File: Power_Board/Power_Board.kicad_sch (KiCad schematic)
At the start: 21 parts, among them J1 Conn_01x10_Female, J2 Conn_01x10_Female, J3 Conn_01x06_Male, J4 Screw_Terminal_01x02, J5 Screw_Terminal_01x02, J6 Conn_01x02_Male

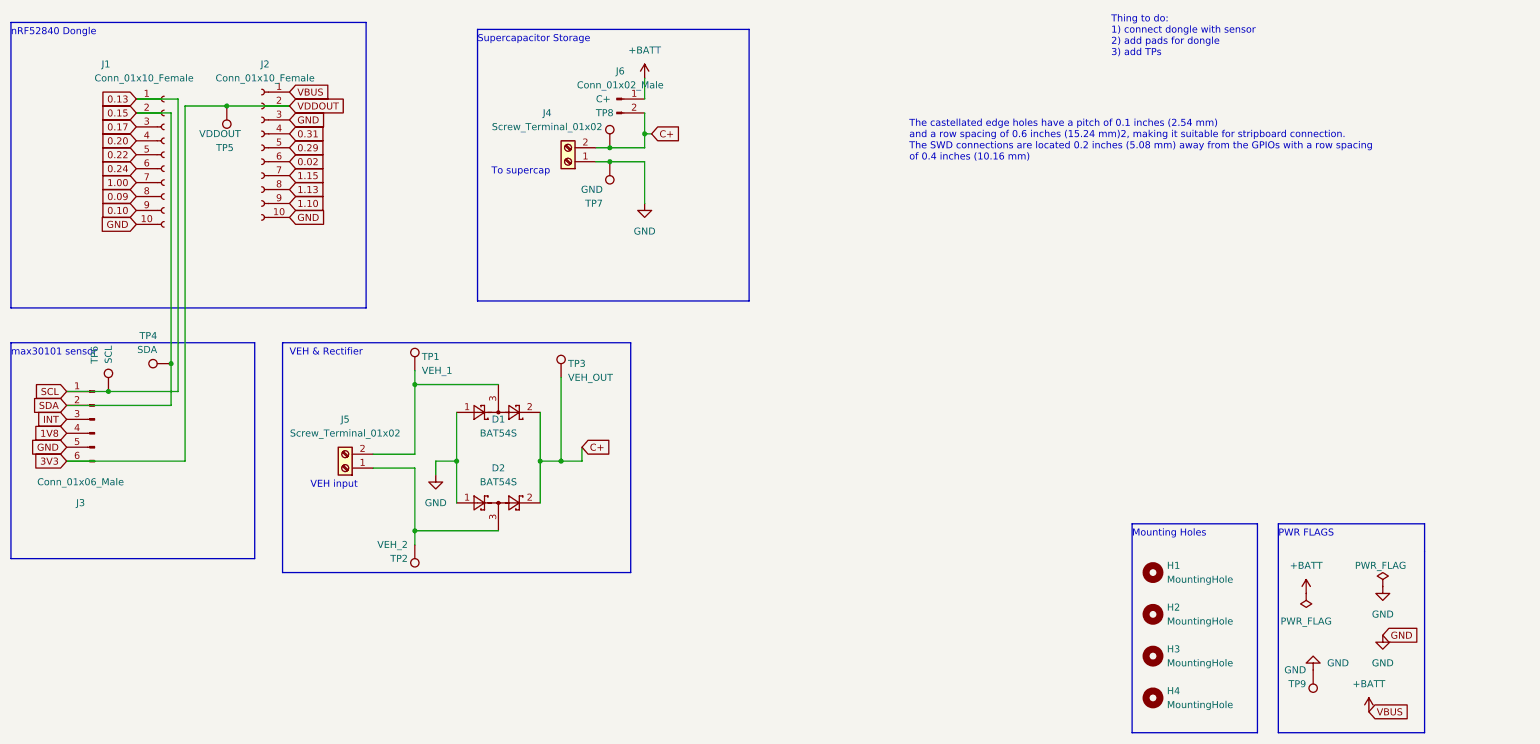
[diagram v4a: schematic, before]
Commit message: silkscreen added
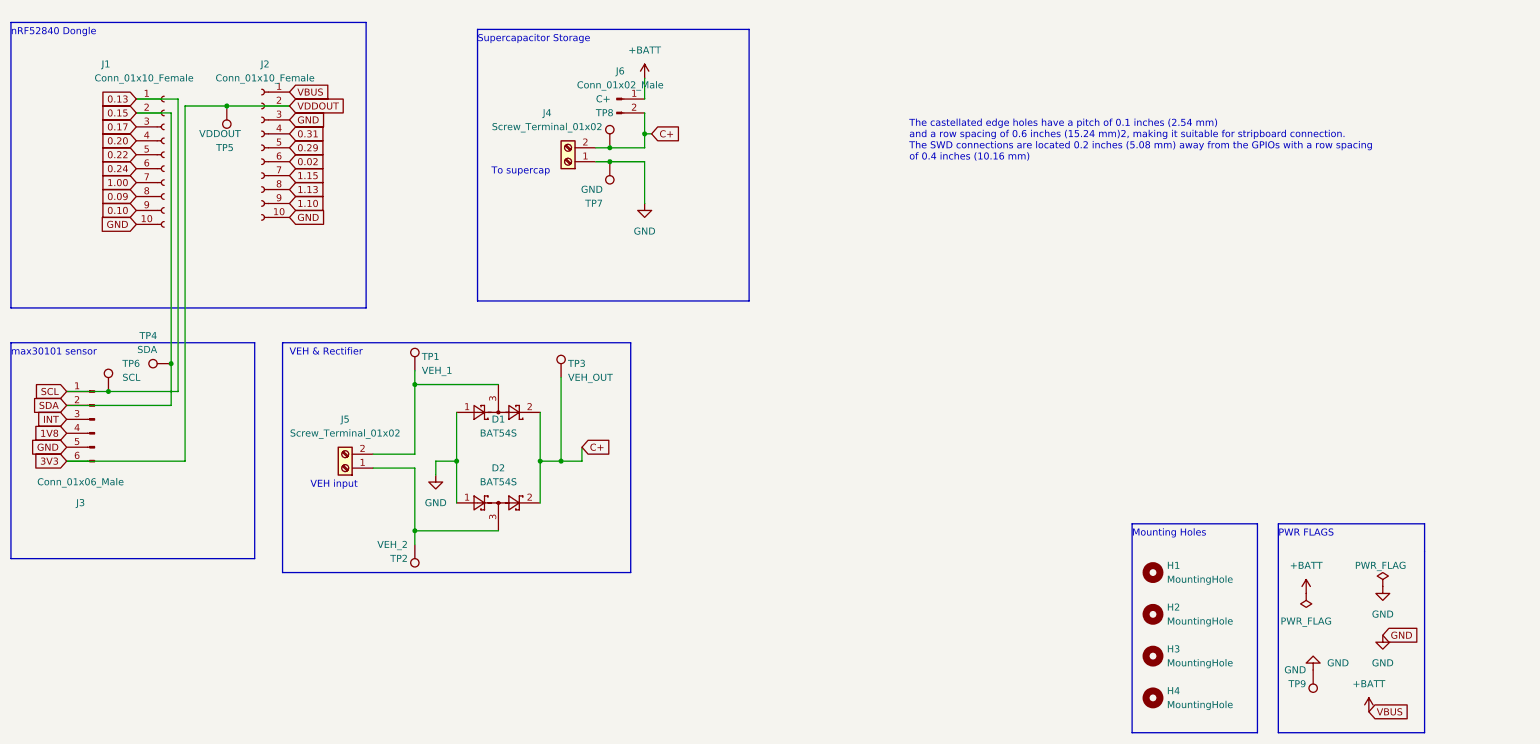
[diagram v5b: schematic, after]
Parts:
- J6: footprint (none) -> Connector_PinHeader_2.54mm:PinHeader_1x02_P2.54mm_Vertical
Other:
- note removed: "Thing to do: 1) connect dongle with sensor 2) add pads for dongle 3) add TPs"
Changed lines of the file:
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@@
-    (effects (font (size 1.27 1.27)) (justify left bottom))
-  )
-  (text "Thing to do:\n1) connect dongle with sensor\n2) add pads for dongle\n3) add TPs\n"
-    (at 227.33 25.4 0)
     (effects (font (size 1.27 1.27)) (justify left bottom))
   )
@@
   (symbol (lib_id "Connector:TestPoint") (at 44.45 86.36 0) (unit 1)
     (in_bom yes) (on_board yes)
-    (property "Reference" "TP6" (id 0) (at 41.91 81.28 90)
-      (effects (font (size 1.27 1.27)) (justify left))
-    )
-    (property "Value" "SCL" (id 1) (at 44.45 81.28 90)
+    (property "Reference" "TP6" (id 0) (at 46.99 81.28 0)
+      (effects (font (size 1.27 1.27)) (justify left))
+    )
+    (property "Value" "SCL" (id 1) (at 46.99 83.82 0)
       (effects (font (size 1.27 1.27)) (justify left))
     )
@@
     (property "Reference" "J6" (id 0) (at 137.795 27.94 0))
     (property "Value" "Conn_01x02_Male" (id 1) (at 137.795 30.48 0))
-    (property "Footprint" "" (id 2) (at 137.16 33.02 0)
-      (effects (font (size 1.27 1.27)) hide)
-    )
+    (property "Footprint" "Connector_PinHeader_2.54mm:PinHeader_1x02_P2.54mm_Vertical" (id 2) (at 137.16 33.02 0)
+      (effects (font (size 1.27 1.27)) hide)
+    )
